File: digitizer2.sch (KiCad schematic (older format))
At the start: 4 parts, among them U1 XC7A35T, U2 FT2232H, U3 MT41K128M16, U4 ADS5403

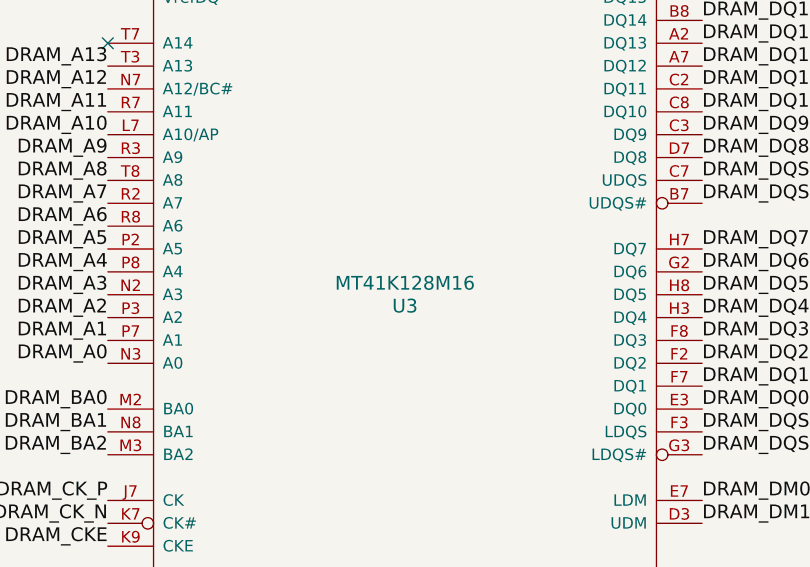
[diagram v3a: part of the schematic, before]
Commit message: Choose final DDR3 part (MT41K and MT41J pin compatible)
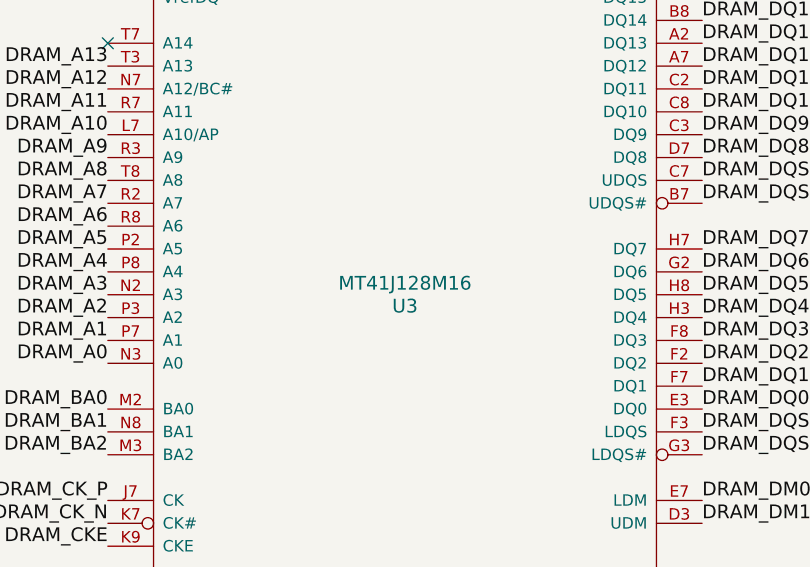
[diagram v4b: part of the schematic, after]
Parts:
- removed U3: MT41K128M16, digitizer2_modules:BGA-96_pitch0.8mm_dia0.35mm, symbol MT41K128M16
- added U3: MT41J128M16, digitizer2_modules:BGA-96_pitch0.8mm_dia0.35mm, symbol MT41J128M16
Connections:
- net DRAM_A0: now also U3.N3 (A0)
- net DRAM_A1: now also U3.P7 (A1)
- net DRAM_A10: now also U3.L7 (A10/AP)
- net DRAM_A11: now also U3.R7 (A11)
- net DRAM_A12: now also U3.N7 (A12/BC#)
- net DRAM_A13: now also U3.T3 (A13)
- net DRAM_A2: now also U3.P3 (A2)
- net DRAM_A3: now also U3.N2 (A3)
- net DRAM_A4: now also U3.P8 (A4)
- net DRAM_A5: now also U3.P2 (A5)
- net DRAM_A6: now also U3.R8 (A6)
- net DRAM_A7: now also U3.R2 (A7)
- net DRAM_A8: now also U3.T8 (A8)
- net DRAM_A9: now also U3.R3 (A9)
- net DRAM_BA0: now also U3.M2 (BA0)
- net DRAM_BA1: now also U3.N8 (BA1)
- net DRAM_BA2: now also U3.M3 (BA2)
- net DRAM_CAS: now also U3.K3 (CAS#)
- net DRAM_CKE: now also U3.K9 (CKE)
- net DRAM_CK_N: now also U3.K7 (CK#)
- net DRAM_CK_P: now also U3.J7 (CK)
- net DRAM_CS: now also U3.L2 (CS#)
- net DRAM_DM0: now also U3.E7 (LDM)
- net DRAM_DM1: now also U3.D3 (UDM)
- net DRAM_DQ0: now also U3.E3 (DQ0)
- net DRAM_DQ1: now also U3.F7 (DQ1)
- net DRAM_DQ10: now also U3.C8 (DQ10)
- net DRAM_DQ11: now also U3.C2 (DQ11)
- net DRAM_DQ12: now also U3.A7 (DQ12)
- net DRAM_DQ13: now also U3.A2 (DQ13)
- net DRAM_DQ14: now also U3.B8 (DQ14)
- net DRAM_DQ15: now also U3.A3 (DQ15)
- net DRAM_DQ2: now also U3.F2 (DQ2)
- net DRAM_DQ3: now also U3.F8 (DQ3)
- net DRAM_DQ4: now also U3.H3 (DQ4)
- net DRAM_DQ5: now also U3.H8 (DQ5)
- net DRAM_DQ6: now also U3.G2 (DQ6)
- net DRAM_DQ7: now also U3.H7 (DQ7)
- net DRAM_DQ8: now also U3.D7 (DQ8)
- net DRAM_DQ9: now also U3.C3 (DQ9)
- net DRAM_DQS0_N: now also U3.G3 (LDQS#)
- net DRAM_DQS0_P: now also U3.F3 (LDQS)
- net DRAM_DQS1_N: now also U3.B7 (UDQS#)
- net DRAM_DQS1_P: now also U3.C7 (UDQS)
- net DRAM_ODT: now also U3.K1 (ODT)
- net DRAM_RAS: now also U3.J3 (RAS#)
- net DRAM_RESET: now also U3.T2 (RESET#)
- net DRAM_WE: now also U3.L3 (WE#)
- net DRAM_ZQ: now also U3.L8 (ZQ)
- new net: U3.A1 (VDDQ), U3.A8 (VDDQ), U3.C1 (VDDQ), U3.C9 (VDDQ), U3.D2 (VDDQ), U3.E9 (VDDQ), U3.F1 (VDDQ), U3.H2 (VDDQ), U3.H9 (VDDQ)
- new net: U3.A9 (VSS), U3.B3 (VSS), U3.E1 (VSS), U3.G8 (VSS), U3.J2 (VSS), U3.J8 (VSS), U3.M1 (VSS), U3.M9 (VSS), U3.P1 (VSS), U3.P9 (VSS), U3.T1 (VSS), U3.T9 (VSS)
- new net: U3.B1 (VSSQ), U3.B9 (VSSQ), U3.D1 (VSSQ), U3.D8 (VSSQ), U3.E2 (VSSQ), U3.E8 (VSSQ), U3.F9 (VSSQ), U3.G1 (VSSQ), U3.G9 (VSSQ)
- new net: U3.B2 (VDD), U3.D9 (VDD), U3.G7 (VDD), U3.K2 (VDD), U3.K8 (VDD), U3.N1 (VDD), U3.N9 (VDD), U3.R1 (VDD), U3.R9 (VDD)
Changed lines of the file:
@@
 LIBS:valves
 LIBS:digitizer2
-LIBS:digitizer2-cache
 EELAYER 25 0
 EELAYER END
@@
 F 3 "" H 2050 11050 60  0000 C CNN
 	1    2050 11050
-	1    0    0    -1
-$EndComp
-$Comp
-L MT41K128M16 U3
-U 1 1 56D5DF5D
-P 5900 11050
-F 0 "U3" H 5900 11000 60  0000 C CNN
-F 1 "MT41K128M16" H 5900 11100 60  0000 C CNN
-F 2 "digitizer2_modules:BGA-96_pitch0.8mm_dia0.35mm" H 5900 11000 60  0001 C CNN
-F 3 "" H 5900 11000 60  0000 C CNN
-	1    5900 11050
 	1    0    0    -1
 $EndComp
@@
 Text Label 13300 1500 0    60   ~ 0
 ADC_SAMPLE_CLK_N
+$Comp
+L MT41J128M16 U3
+U 1 1 56E6EDF3
+P 5900 11050
+F 0 "U3" H 5900 11000 60  0000 C CNN
+F 1 "MT41J128M16" H 5900 11100 60  0000 C CNN
+F 2 "digitizer2_modules:BGA-96_pitch0.8mm_dia0.35mm" H 5900 11000 60  0001 C CNN
+F 3 "" H 5900 11000 60  0000 C CNN
+	1    5900 11050
+	1    0    0    -1
+$EndComp
 $EndSCHEMATC

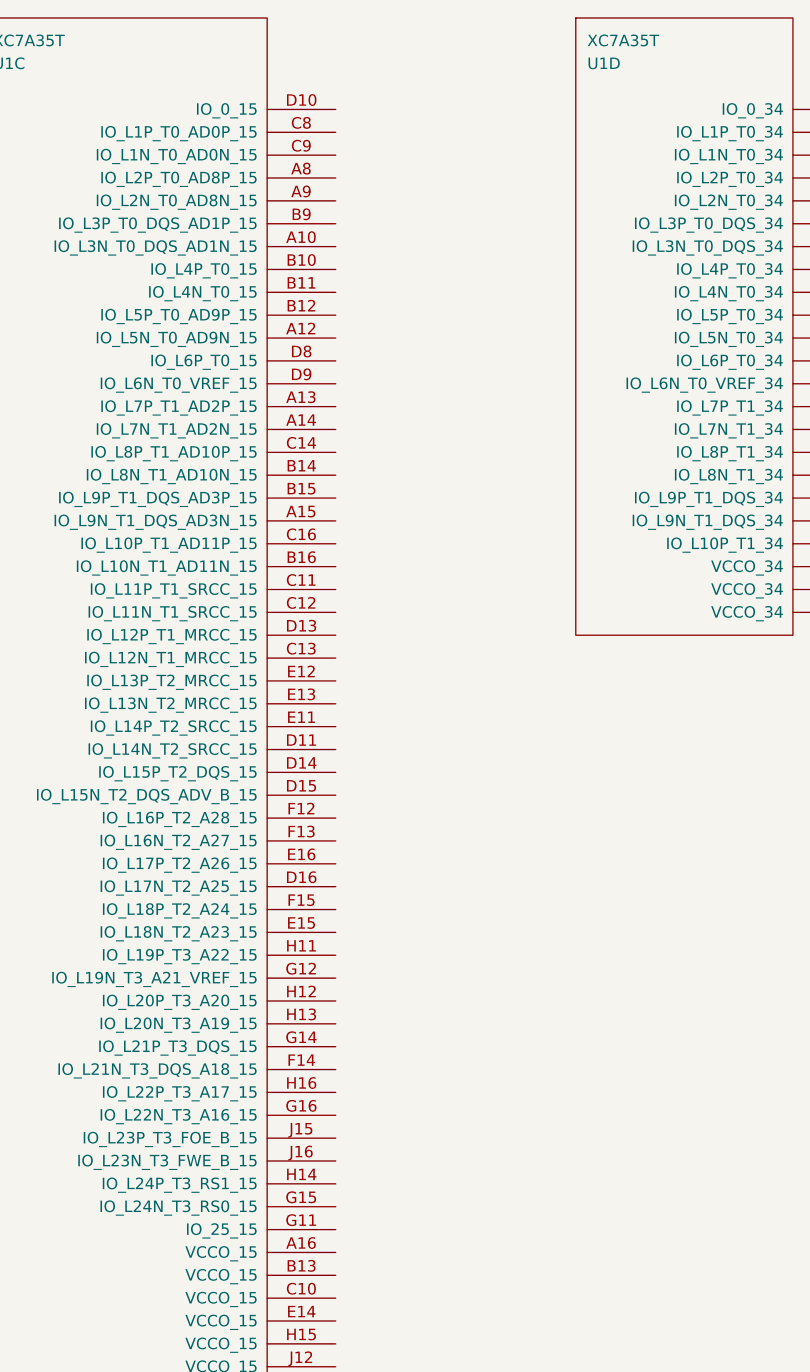
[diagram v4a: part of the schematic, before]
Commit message: DDR DQ lanes routing
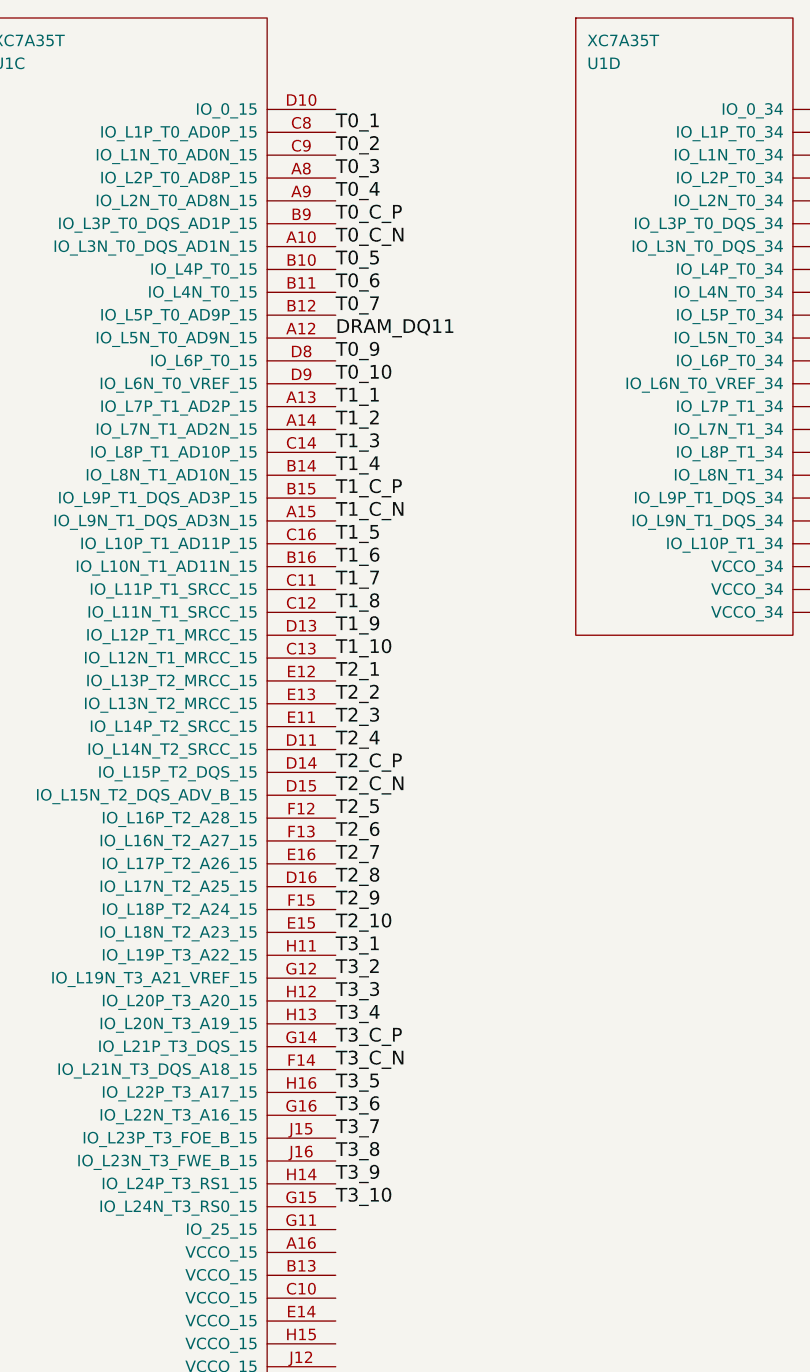
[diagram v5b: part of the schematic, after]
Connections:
- net DRAM_DQ11: now also U1.A12 (IO_L5N_T0_AD9N_15)
- net T0_C_N: now reaches U1.A10 (IO_L3N_T0_DQS_AD1N_15)
- net T1_1: now reaches U1.A13 (IO_L7P_T1_AD2P_15)
- net T1_2: now reaches U1.A14 (IO_L7N_T1_AD2N_15)
- net T1_C_N: now reaches U1.A15 (IO_L9N_T1_DQS_AD3N_15)
- net T0_3: now reaches U1.A8 (IO_L2P_T0_AD8P_15)
- net T0_4: now reaches U1.A9 (IO_L2N_T0_AD8N_15)
- net T0_5: now reaches U1.B10 (IO_L4P_T0_15)
- net T0_6: now reaches U1.B11 (IO_L4N_T0_15)
- net T0_7: now reaches U1.B12 (IO_L5P_T0_AD9P_15)
- net T1_4: now reaches U1.B14 (IO_L8N_T1_AD10N_15)
- net T1_C_P: now reaches U1.B15 (IO_L9P_T1_DQS_AD3P_15)
- net T1_6: now reaches U1.B16 (IO_L10N_T1_AD11N_15)
- net T0_C_P: now reaches U1.B9 (IO_L3P_T0_DQS_AD1P_15)
- net T1_7: now reaches U1.C11 (IO_L11P_T1_SRCC_15)
- net T1_8: now reaches U1.C12 (IO_L11N_T1_SRCC_15)
- net T1_10: now reaches U1.C13 (IO_L12N_T1_MRCC_15)
- net T1_3: now reaches U1.C14 (IO_L8P_T1_AD10P_15)
- net T1_5: now reaches U1.C16 (IO_L10P_T1_AD11P_15)
- net T0_1: now reaches U1.C8 (IO_L1P_T0_AD0P_15)
- net T0_2: now reaches U1.C9 (IO_L1N_T0_AD0N_15)
- net T2_4: now reaches U1.D11 (IO_L14N_T2_SRCC_15)
- net T1_9: now reaches U1.D13 (IO_L12P_T1_MRCC_15)
- net T2_C_P: now reaches U1.D14 (IO_L15P_T2_DQS_15)
- net T2_C_N: now reaches U1.D15 (IO_L15N_T2_DQS_ADV_B_15)
- net T2_8: now reaches U1.D16 (IO_L17N_T2_A25_15)
- net T0_9: now reaches U1.D8 (IO_L6P_T0_15)
- net T0_10: now reaches U1.D9 (IO_L6N_T0_VREF_15)
- net T2_3: now reaches U1.E11 (IO_L14P_T2_SRCC_15)
- net T2_1: now reaches U1.E12 (IO_L13P_T2_MRCC_15)
- net T2_2: now reaches U1.E13 (IO_L13N_T2_MRCC_15)
- net T2_10: now reaches U1.E15 (IO_L18N_T2_A23_15)
- net T2_7: now reaches U1.E16 (IO_L17P_T2_A26_15)
- net T2_5: now reaches U1.F12 (IO_L16P_T2_A28_15)
- net T2_6: now reaches U1.F13 (IO_L16N_T2_A27_15)
- net T3_C_N: now reaches U1.F14 (IO_L21N_T3_DQS_A18_15)
- net T2_9: now reaches U1.F15 (IO_L18P_T2_A24_15)
- net T3_2: now reaches U1.G12 (IO_L19N_T3_A21_VREF_15)
- net T3_C_P: now reaches U1.G14 (IO_L21P_T3_DQS_15)
- net T3_10: now reaches U1.G15 (IO_L24N_T3_RS0_15)
- net T3_6: now reaches U1.G16 (IO_L22N_T3_A16_15)
- net T3_1: now reaches U1.H11 (IO_L19P_T3_A22_15)
- net T3_3: now reaches U1.H12 (IO_L20P_T3_A20_15)
- net T3_4: now reaches U1.H13 (IO_L20N_T3_A19_15)
- net T3_9: now reaches U1.H14 (IO_L24P_T3_RS1_15)
- net T3_5: now reaches U1.H16 (IO_L22P_T3_A17_15)
- net T3_7: now reaches U1.J15 (IO_L23P_T3_FOE_B_15)
- net T3_8: now reaches U1.J16 (IO_L23N_T3_FWE_B_15)
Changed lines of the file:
@@
 LIBS:valves
 LIBS:digitizer2
+LIBS:digitizer2-cache
 EELAYER 25 0
 EELAYER END
@@
 	1    0    0    -1
 $EndComp
+Text Label 6950 1000 0    60   ~ 0
+T0_1
+Text Label 6950 1100 0    60   ~ 0
+T0_2
+Text Label 6950 1200 0    60   ~ 0
+T0_3
+Text Label 6950 1300 0    60   ~ 0
+T0_4
+Text Label 6950 1400 0    60   ~ 0
+T0_C_P
+Text Label 6950 1500 0    60   ~ 0
+T0_C_N
+Text Label 6950 1600 0    60   ~ 0
+T0_5
+Text Label 6950 1700 0    60   ~ 0
+T0_6
+Text Label 6950 1800 0    60   ~ 0
+T0_7
+Text Label 6950 1900 0    60   ~ 0
+DRAM_DQ11
+Text Label 6950 2000 0    60   ~ 0
+T0_9
+Text Label 6950 2100 0    60   ~ 0
+T0_10
+Text Label 6950 2200 0    60   ~ 0
+T1_1
+Text Label 6950 2300 0    60   ~ 0
+T1_2
+Text Label 6950 2400 0    60   ~ 0
+T1_3
+Text Label 6950 2500 0    60   ~ 0
+T1_4
+Text Label 6950 2800 0    60   ~ 0
+T1_5
+Text Label 6950 2900 0    60   ~ 0
+T1_6
+Text Label 6950 3000 0    60   ~ 0
+T1_7
+Text Label 6950 3100 0    60   ~ 0
+T1_8
+Text Label 6950 3200 0    60   ~ 0
+T1_9
+Text Label 6950 3300 0    60   ~ 0
+T1_10
+Text Label 6950 3400 0    60   ~ 0
+T2_1
+Text Label 6950 3500 0    60   ~ 0
+T2_2
+Text Label 6950 3600 0    60   ~ 0
+T2_3
+Text Label 6950 3700 0    60   ~ 0
+T2_4
+Text Label 6950 4000 0    60   ~ 0
+T2_5
+Text Label 6950 4100 0    60   ~ 0
+T2_6
+Text Label 6950 4200 0    60   ~ 0
+T2_7
+Text Label 6950 4300 0    60   ~ 0
+T2_8
+Text Label 6950 4400 0    60   ~ 0
+T2_9
+Text Label 6950 4500 0    60   ~ 0
+T2_10
+Text Label 6950 3800 0    60   ~ 0
+T2_C_P
+Text Label 6950 3900 0    60   ~ 0
+T2_C_N
+Text Label 6950 2600 0    60   ~ 0
+T1_C_P
+Text Label 6950 2700 0    60   ~ 0
+T1_C_N
+Text Label 6950 4600 0    60   ~ 0
+T3_1
+Text Label 6950 4700 0    60   ~ 0
+T3_2
+Text Label 6950 4800 0    60   ~ 0
+T3_3
+Text Label 6950 4900 0    60   ~ 0
+T3_4
+Text Label 6950 5000 0    60   ~ 0
+T3_C_P
+Text Label 6950 5100 0    60   ~ 0
+T3_C_N
+Text Label 6950 5200 0    60   ~ 0
+T3_5
+Text Label 6950 5300 0    60   ~ 0
+T3_6
+Text Label 6950 5400 0    60   ~ 0
+T3_7
+Text Label 6950 5500 0    60   ~ 0
+T3_8
+Text Label 6950 5600 0    60   ~ 0
+T3_9
+Text Label 6950 5700 0    60   ~ 0
+T3_10
 $EndSCHEMATC

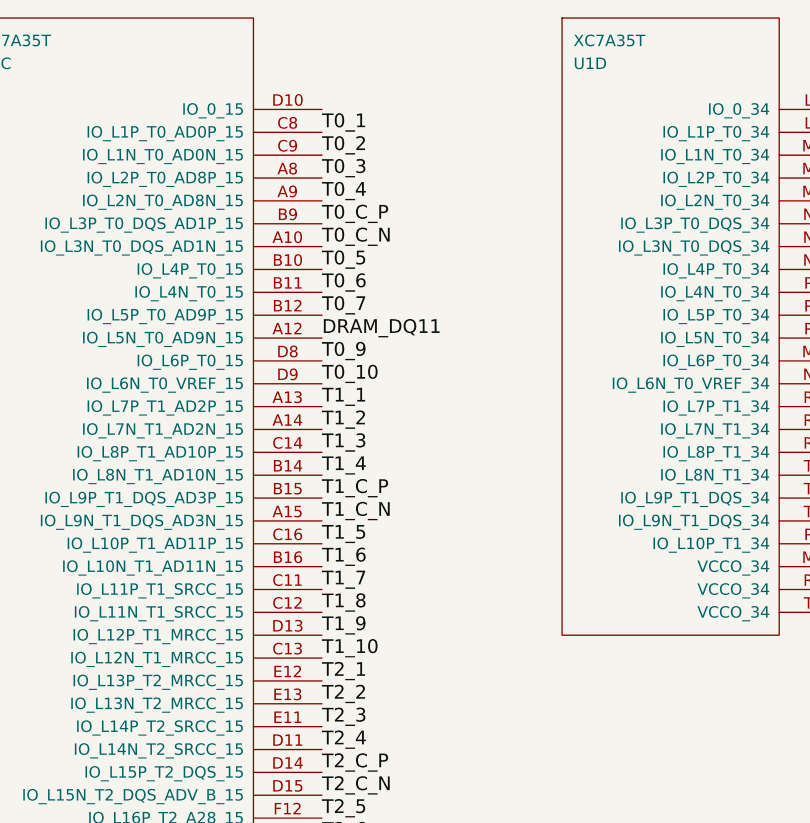
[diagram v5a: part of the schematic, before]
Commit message: Finished DRAM DQ groups
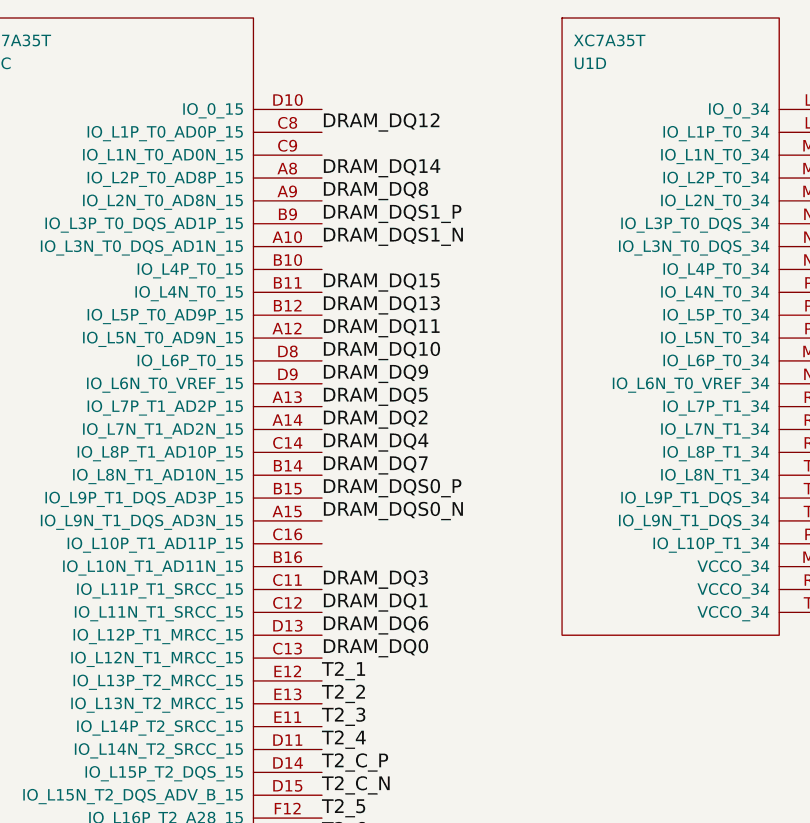
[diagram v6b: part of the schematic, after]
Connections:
- net T0_1 is gone; now on net DRAM_DQ12: U1.C8 (IO_L1P_T0_AD0P_15)
- net T0_10 is gone; now on net DRAM_DQ9: U1.D9 (IO_L6N_T0_VREF_15)
- net T0_3 is gone; now on net DRAM_DQ14: U1.A8 (IO_L2P_T0_AD8P_15)
- net T0_4 is gone; now on net DRAM_DQ8: U1.A9 (IO_L2N_T0_AD8N_15)
- net T0_6 is gone; now on net DRAM_DQ15: U1.B11 (IO_L4N_T0_15)
- net T0_7 is gone; now on net DRAM_DQ13: U1.B12 (IO_L5P_T0_AD9P_15)
- net T0_9 is gone; now on net DRAM_DQ10: U1.D8 (IO_L6P_T0_15)
- net T0_C_N is gone; now on net DRAM_DQS1_N: U1.A10 (IO_L3N_T0_DQS_AD1N_15)
- net T0_C_P is gone; now on net DRAM_DQS1_P: U1.B9 (IO_L3P_T0_DQS_AD1P_15)
- net T1_1 is gone; now on net DRAM_DQ5: U1.A13 (IO_L7P_T1_AD2P_15)
- net T1_10 is gone; now on net DRAM_DQ0: U1.C13 (IO_L12N_T1_MRCC_15)
- net T1_2 is gone; now on net DRAM_DQ2: U1.A14 (IO_L7N_T1_AD2N_15)
- net T1_3 is gone; now on net DRAM_DQ4: U1.C14 (IO_L8P_T1_AD10P_15)
- net T1_4 is gone; now on net DRAM_DQ7: U1.B14 (IO_L8N_T1_AD10N_15)
- net T1_7 is gone; now on net DRAM_DQ3: U1.C11 (IO_L11P_T1_SRCC_15)
- net T1_8 is gone; now on net DRAM_DQ1: U1.C12 (IO_L11N_T1_SRCC_15)
- net T1_9 is gone; now on net DRAM_DQ6: U1.D13 (IO_L12P_T1_MRCC_15)
- net T1_C_N is gone; now on net DRAM_DQS0_N: U1.A15 (IO_L9N_T1_DQS_AD3N_15)
- net T1_C_P is gone; now on net DRAM_DQS0_P: U1.B15 (IO_L9P_T1_DQS_AD3P_15)
- net T0_2: no longer names the net of U1.C9 (IO_L1N_T0_AD0N_15)
- net T0_5: no longer names the net of U1.B10 (IO_L4P_T0_15)
- net T1_5: no longer names the net of U1.C16 (IO_L10P_T1_AD11P_15)
- net T1_6: no longer names the net of U1.B16 (IO_L10N_T1_AD11N_15)
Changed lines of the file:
@@
 $EndComp
 Text Label 6950 1000 0    60   ~ 0
-T0_1
-Text Label 6950 1100 0    60   ~ 0
-T0_2
+DRAM_DQ12
 Text Label 6950 1200 0    60   ~ 0
-T0_3
+DRAM_DQ14
 Text Label 6950 1300 0    60   ~ 0
-T0_4
+DRAM_DQ8
 Text Label 6950 1400 0    60   ~ 0
-T0_C_P
+DRAM_DQS1_P
 Text Label 6950 1500 0    60   ~ 0
-T0_C_N
-Text Label 6950 1600 0    60   ~ 0
-T0_5
+DRAM_DQS1_N
 Text Label 6950 1700 0    60   ~ 0
-T0_6
+DRAM_DQ15
 Text Label 6950 1800 0    60   ~ 0
-T0_7
+DRAM_DQ13
 Text Label 6950 1900 0    60   ~ 0
 DRAM_DQ11
 Text Label 6950 2000 0    60   ~ 0
-T0_9
+DRAM_DQ10
 Text Label 6950 2100 0    60   ~ 0
-T0_10
+DRAM_DQ9
 Text Label 6950 2200 0    60   ~ 0
-T1_1
+DRAM_DQ5
 Text Label 6950 2300 0    60   ~ 0
-T1_2
+DRAM_DQ2
 Text Label 6950 2400 0    60   ~ 0
-T1_3
+DRAM_DQ4
 Text Label 6950 2500 0    60   ~ 0
-T1_4
-Text Label 6950 2800 0    60   ~ 0
-T1_5
-Text Label 6950 2900 0    60   ~ 0
-T1_6
+DRAM_DQ7
 Text Label 6950 3000 0    60   ~ 0
-T1_7
+DRAM_DQ3
 Text Label 6950 3100 0    60   ~ 0
-T1_8
+DRAM_DQ1
 Text Label 6950 3200 0    60   ~ 0
-T1_9
+DRAM_DQ6
 Text Label 6950 3300 0    60   ~ 0
-T1_10
+DRAM_DQ0
 Text Label 6950 3400 0    60   ~ 0
 T2_1
@@
 T2_C_N
 Text Label 6950 2600 0    60   ~ 0
-T1_C_P
+DRAM_DQS0_P
 Text Label 6950 2700 0    60   ~ 0
-T1_C_N
+DRAM_DQS0_N
 Text Label 6950 4600 0    60   ~ 0
 T3_1
